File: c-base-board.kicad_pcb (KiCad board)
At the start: 2 copper layers, 49.1 x 49.1 mm, 172 parts

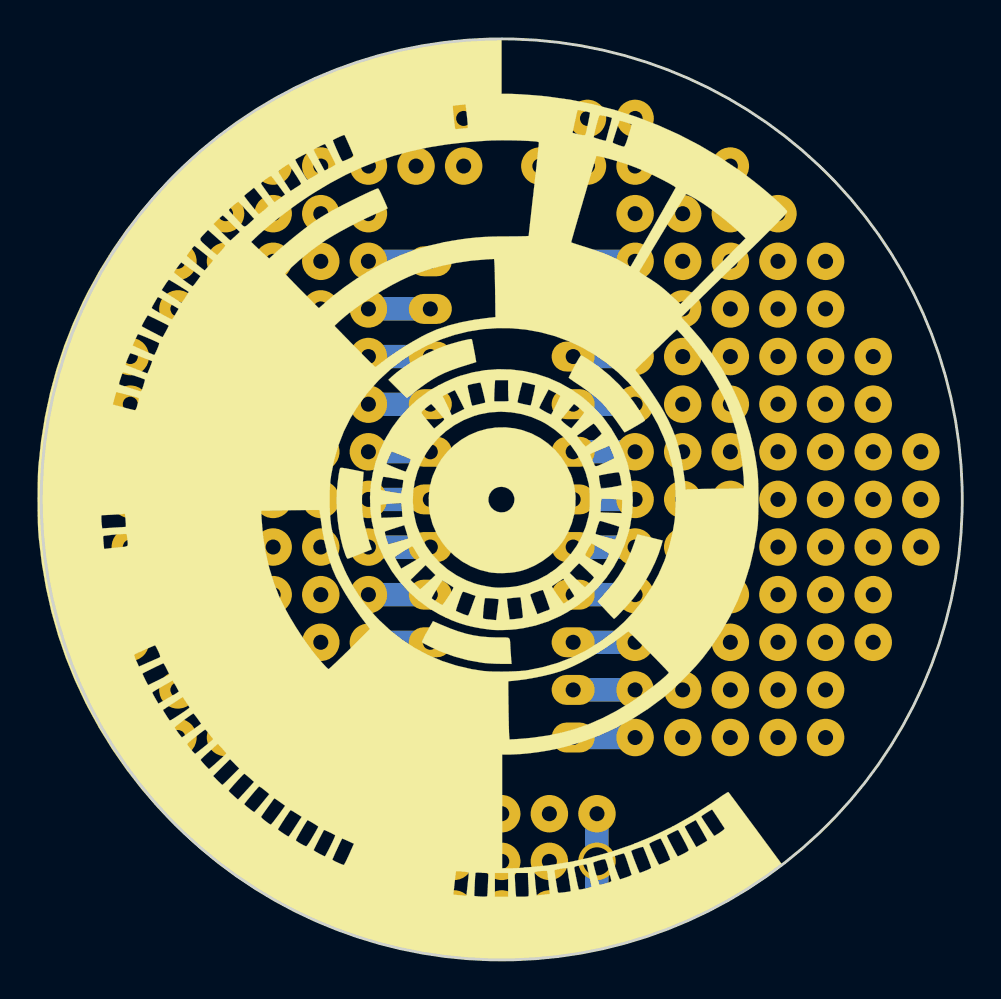
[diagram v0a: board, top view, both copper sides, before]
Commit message: improved revision
* 7805 support on bottom part
* ground and regulated volate bar at the sides
* no support for DIP28 packages
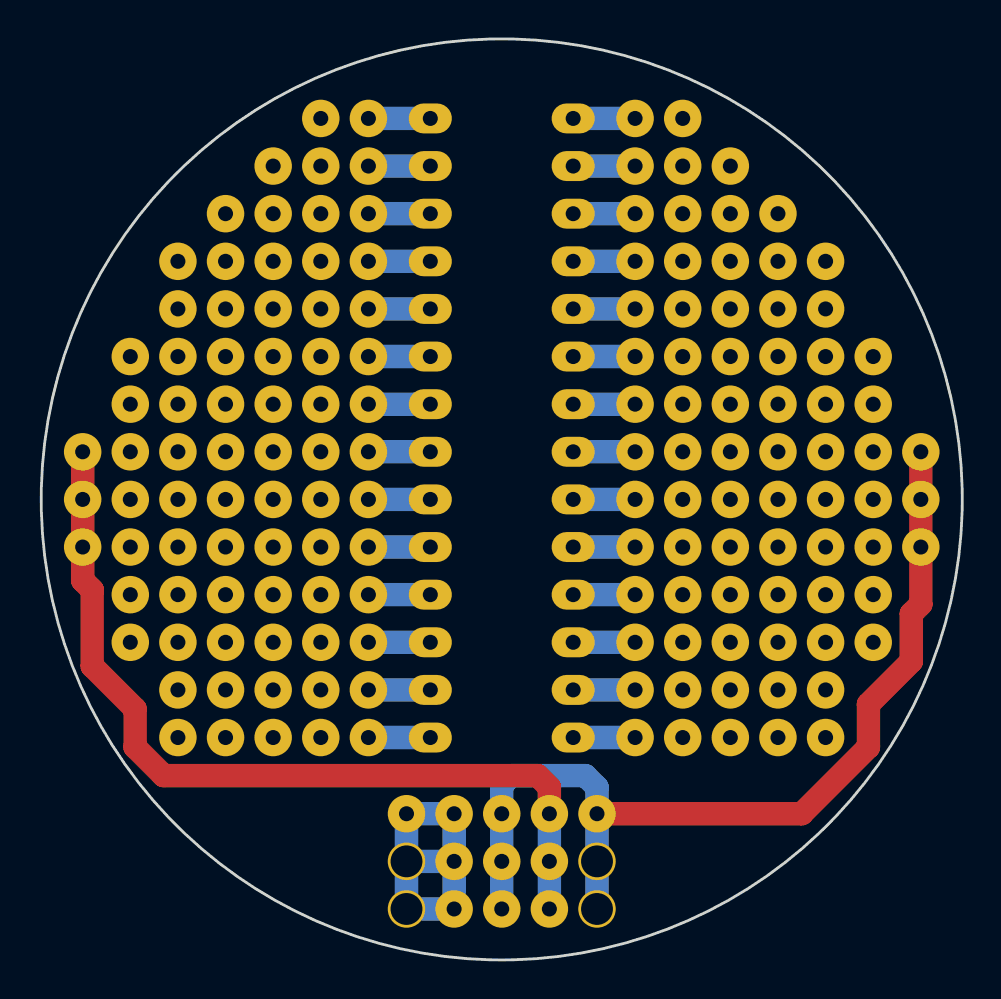
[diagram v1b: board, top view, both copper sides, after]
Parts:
- removed the G*** at (149.1, 123.4)
- removed the REF** at (145.3, 136.1)
- removed the REF**11 at (151.1, 103.1)
- removed the REF**11 at (153.7, 103.1)
- removed the REF**11 at (147.1, 103.1)
- removed the REF**11 at (147.1, 105.7)
- removed the REF**11 at (151.1, 105.7)
- removed the REF**11 at (153.7, 105.7)
- removed the REF**41 at (144.5, 103.1)
- removed the REF**41 at (144.5, 105.7)
- added REF**: DIP-28_W7.62mm_LongPads, Housings_DIP:DIP-28_W7.62mm_LongPads, B.Cu at (145.3, 136.1)
- added REF**21: SolderWirePad_single_0-8mmDrill, Wire_Pads:SolderWirePad_single_0-8mmDrill, F.Cu at (158.8, 103.1)
- added REF**31: SolderWirePad_single_0-8mmDrill, Wire_Pads:SolderWirePad_single_0-8mmDrill, F.Cu at (139.4, 103.1)
- moved G*** 3.05 mm to (149.1, 120.4)
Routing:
- net (no net): track 82.8 -> 208.1 mm
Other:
- board text added: "+"
- board text added: "rev-C"
- board text added: "⏚"
- board text removed: "rev-c"

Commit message: added c-base silkscreen
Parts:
- added G***: c-base, c-base-board:board-outline, F.Cu at (149.4, 123.4)

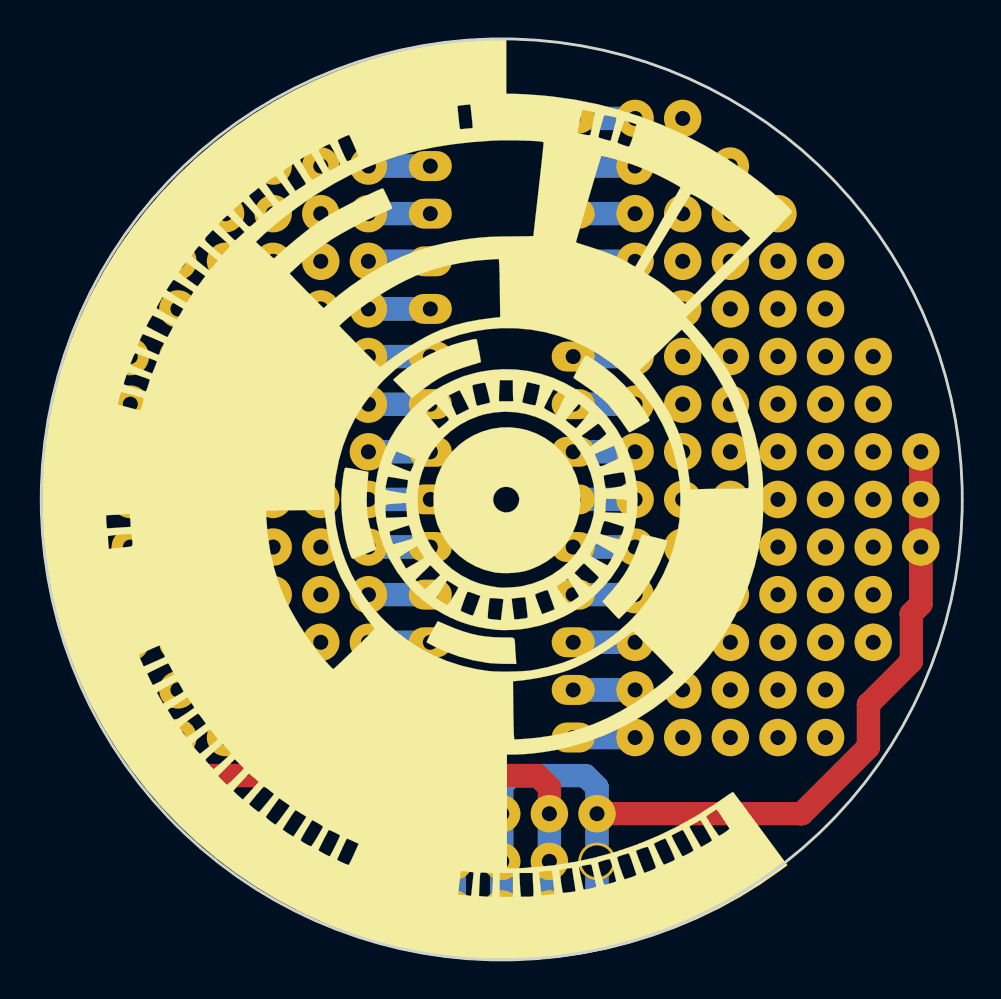
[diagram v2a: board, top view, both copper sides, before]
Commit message: added jumper spots for GND in voltage regulator area
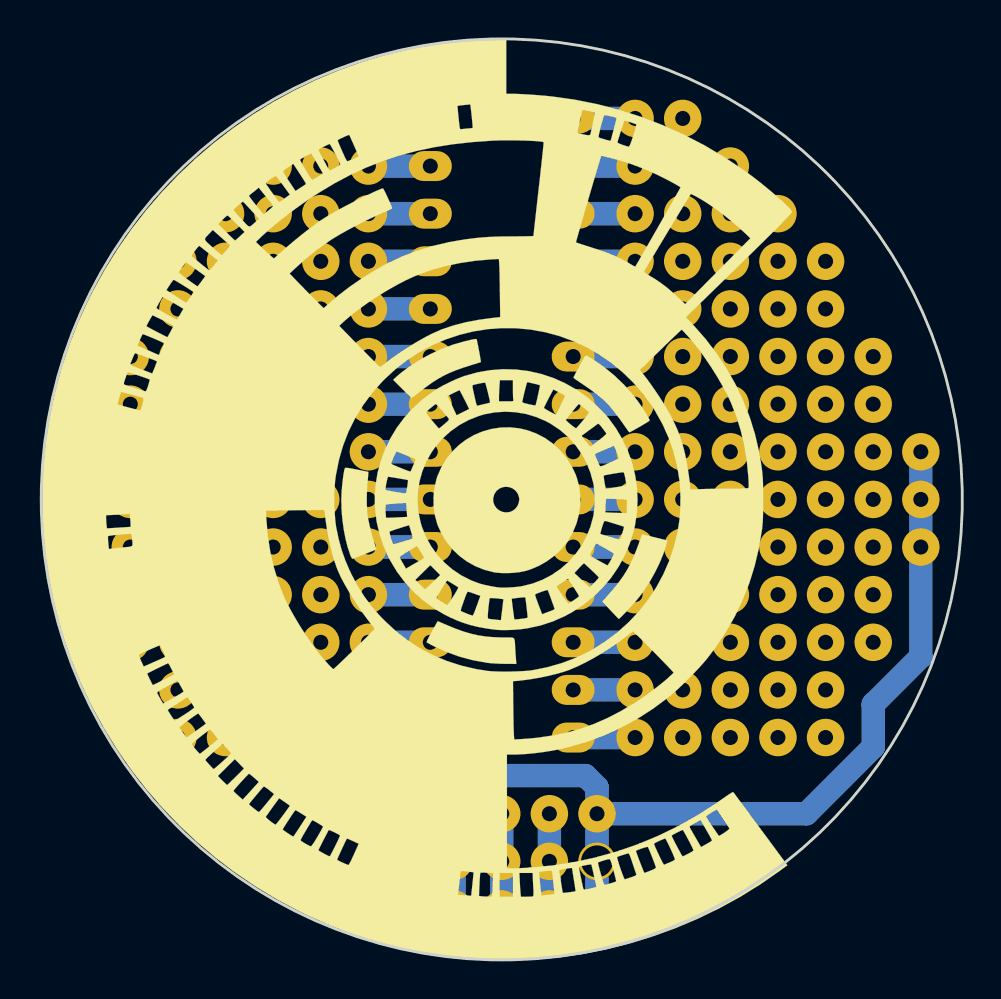
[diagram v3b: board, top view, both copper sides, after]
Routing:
- net (no net): track 208.1 -> 165.2 mm
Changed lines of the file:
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@@
     (area 124.461199 98.807199 173.734801 148.080801)
     (thickness 1.6)
-    (drawings 32)
-    (tracks 66)
+    (drawings 22)
+    (tracks 50)
     (zones 0)
     (modules 166)
@@
     (35 F.Paste user hide)
     (36 B.SilkS user)
-    (37 F.SilkS user)
-    (38 B.Mask user hide)
-    (39 F.Mask user hide)
+    (37 F.SilkS user hide)
+    (38 B.Mask user)
+    (39 F.Mask user)
     (40 Dwgs.User user hide)
     (41 Cmts.User user hide)
@@
       (xy -0.319227 -3.833328) (xy 0.178311 -3.845117) (xy 0.680572 -3.791698)) (layer F.SilkS) (width 0.01))
   )
+  (gr_text ⏚ (at 171.45 127.762) (layer B.SilkS)
+    (effects (font (size 1 1) (thickness 0.2)) (justify mirror))
+  )
+  (gr_line (start 151.638 138.938) (end 151.638 137.922) (layer B.Mask) (width 1))
+  (gr_line (start 149.098 138.938) (end 149.098 137.922) (layer B.Mask) (width 1))
+  (gr_line (start 146.558 138.938) (end 146.558 137.922) (layer B.Mask) (width 1))
   (dimension 49.276 (width 0.3) (layer Eco1.User)
     (gr_text "49,276 mm" (at 183.722 123.444 270) (layer Eco1.User)
@@
     (arrow2b (pts (xy 173.736 94.742) (xy 172.609496 95.328421)))
   )
-  (gr_line (start 126.746 129.794) (end 126.746 127.254) (layer B.SilkS) (width 0.2))
-  (gr_line (start 129.54 136.398) (end 126.746 129.794) (layer B.SilkS) (width 0.2))
-  (gr_line (start 131.064 137.922) (end 129.54 136.398) (layer B.SilkS) (width 0.2))
-  (gr_line (start 142.748 137.922) (end 131.064 137.922) (layer B.SilkS) (width 0.2))
-  (gr_line (start 142.748 138.938) (end 142.748 137.922) (layer B.SilkS) (width 0.2))
-  (gr_line (start 151.638 138.938) (end 142.748 138.938) (layer B.SilkS) (width 0.2))
-  (gr_line (start 151.638 139.192) (end 151.638 138.938) (layer B.SilkS) (width 0.2))
-  (gr_line (start 154.178 137.668) (end 154.178 138.938) (layer B.SilkS) (width 0.2))
-  (gr_line (start 155.448 137.668) (end 154.178 137.668) (layer B.SilkS) (width 0.2))
-  (gr_line (start 167.386 137.668) (end 155.448 137.668) (layer B.SilkS) (width 0.2))
-  (gr_line (start 170.688 132.334) (end 167.386 137.668) (layer B.SilkS) (width 0.2))
-  (gr_line (start 171.45 127.254) (end 170.688 132.334) (layer B.SilkS) (width 0.2))
-  (gr_text ⏚ (at 149.098 147.066) (layer B.SilkS)
+  (gr_text ⏚ (at 154.178 146.812) (layer B.SilkS)
     (effects (font (size 1 1) (thickness 0.2)) (justify mirror))
   )
-  (gr_text ⏚ (at 155.7274 138.2522) (layer B.SilkS)
-    (effects (font (size 1 1) (thickness 0.2)) (justify mirror))
-  )
-  (gr_text + (at 145.288 141.478) (layer B.SilkS)
+  (gr_text + (at 144.018 146.558) (layer B.SilkS)
     (effects (font (size 1 1) (thickness 0.2)) (justify mirror))
   )
@@
   (gr_line (start 125.476 119.634) (end 125.476 127.254) (layer B.SilkS) (width 0.2))
   (gr_line (start 170.18 127.254) (end 172.72 127.254) (layer B.SilkS) (width 0.2))
-  (gr_text + (at 145.288 144.018) (layer B.SilkS)
-    (effects (font (size 1 1) (thickness 0.2)) (justify mirror))
-  )
   (gr_text rev-C (at 138.684 141.478) (layer B.SilkS)
     (effects (font (size 1.5 1.5) (thickness 0.3)) (justify mirror))
@@
   )
   (gr_circle (center 149.098 123.444) (end 149.098 98.8822) (layer Edge.Cuts) (width 0.15))
-  (segment (start 144.018 142.748) (end 146.558 142.748) (width 1.25) (layer B.Cu) (net 0))
-  (segment (start 154.178 140.208) (end 165.1 140.208) (width 1.25) (layer F.Cu) (net 0))
-  (segment (start 165.1 140.208) (end 168.656 136.652) (width 1.25) (layer F.Cu) (net 0))
-  (segment (start 168.656 136.652) (end 168.656 134.366) (width 1.25) (layer F.Cu) (net 0))
-  (segment (start 168.656 134.366) (end 170.942 132.08) (width 1.25) (layer F.Cu) (net 0))
-  (segment (start 171.45 129.032) (end 171.45 125.984) (width 1.25) (layer F.Cu) (net 0))
-  (segment (start 170.942 132.08) (end 170.942 129.54) (width 1.25) (layer F.Cu) (net 0))
-  (segment (start 170.942 129.54) (end 171.45 129.032) (width 1.25) (layer F.Cu) (net 0))
-  (segment (start 126.746 125.984) (end 126.746 127.762) (width 1.25) (layer F.Cu) (net 0))
-  (segment (start 126.746 127.762) (end 127.254 128.27) (width 1.25) (layer F.Cu) (net 0))
-  (segment (start 151.019492 138.176) (end 151.638 138.794508) (width 1.25) (layer F.Cu) (net 0))
-  (segment (start 127.254 128.27) (end 127.254 132.334) (width 1.25) (layer F.Cu) (net 0))
-  (segment (start 127.254 132.334) (end 129.54 134.62) (width 1.25) (layer F.Cu) (net 0))
-  (segment (start 129.54 134.62) (end 129.54 136.652) (width 1.25) (layer F.Cu) (net 0))
-  (segment (start 151.638 138.794508) (end 151.638 140.208) (width 1.25) (layer F.Cu) (net 0))
-  (segment (start 129.54 136.652) (end 131.064 138.176) (width 1.25) (layer F.Cu) (net 0))
-  (segment (start 131.064 138.176) (end 151.019492 138.176) (width 1.25) (layer F.Cu) (net 0))
-  (segment (start 149.606 138.176) (end 149.098 138.684) (width 1.25) (layer B.Cu) (net 0))
-  (segment (start 149.098 138.684) (end 149.098 140.208) (width 1.25) (layer B.Cu) (net 0))
-  (segment (start 153.559492 138.176) (end 149.606 138.176) (width 1.25) (layer B.Cu) (net 0))
+  (segment (start 153.559492 138.176) (end 146.558 138.176) (width 1.25) (layer B.Cu) (net 0))
   (segment (start 154.178 140.208) (end 154.178 138.794508) (width 1.25) (layer B.Cu) (net 0))
   (segment (start 154.178 138.794508) (end 153.559492 138.176) (width 1.25) (layer B.Cu) (net 0))
-  (segment (start 126.746 123.444) (end 126.746 120.904) (width 1.25) (layer F.Cu) (net 0))
-  (segment (start 126.746 125.984) (end 126.746 123.444) (width 1.25) (layer F.Cu) (net 0))
-  (segment (start 171.45 123.444) (end 171.45 120.904) (width 1.25) (layer F.Cu) (net 0))
-  (segment (start 171.45 125.984) (end 171.45 123.444) (width 1.25) (layer F.Cu) (net 0))
+  (segment (start 154.178 140.208) (end 165.354 140.208) (width 1.25) (layer B.Cu) (net 0))
+  (segment (start 168.91 136.652) (end 168.91 134.366) (width 1.25) (layer B.Cu) (net 0))
+  (segment (start 168.91 134.366) (end 171.45 131.826) (width 1.25) (layer B.Cu) (net 0))
+  (segment (start 165.354 140.208) (end 168.91 136.652) (width 1.25) (layer B.Cu) (net 0))
+  (segment (start 171.45 131.826) (end 171.45 125.984) (width 1.25) (layer B.Cu) (net 0))
+  (segment (start 126.746 123.444) (end 126.746 125.984) (width 1.25) (layer B.Cu) (net 0))
+  (segment (start 126.746 120.904) (end 126.746 123.444) (width 1.25) (layer B.Cu) (net 0))
+  (segment (start 171.45 125.984) (end 171.45 123.444) (width 1.25) (layer B.Cu) (net 0))
+  (segment (start 171.45 120.904) (end 171.45 123.444) (width 1.25) (layer B.Cu) (net 0))
   (segment (start 145.288 136.144) (end 141.986 136.144) (width 1.25) (layer B.Cu) (net 0))
   (segment (start 141.986 133.604) (end 145.288 133.604) (width 1.25) (layer B.Cu) (net 0))
@@
   (segment (start 152.908 133.604) (end 156.21 133.604) (width 1.25) (layer B.Cu) (net 0))
   (segment (start 152.908 136.144) (end 156.21 136.144) (width 1.25) (layer B.Cu) (net 0))
-  (segment (start 144.018 145.288) (end 146.558 145.288) (width 1.25) (layer B.Cu) (net 0))
-  (segment (start 144.018 140.208) (end 146.558 140.208) (width 1.25) (layer B.Cu) (net 0))
   (segment (start 144.018 142.748) (end 144.018 140.208) (width 1.25) (layer B.Cu) (net 0))
   (segment (start 151.638 142.748) (end 151.638 140.208) (width 1.25) (layer B.Cu) (net 0))

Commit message: new revision - orderd from dirtypcb
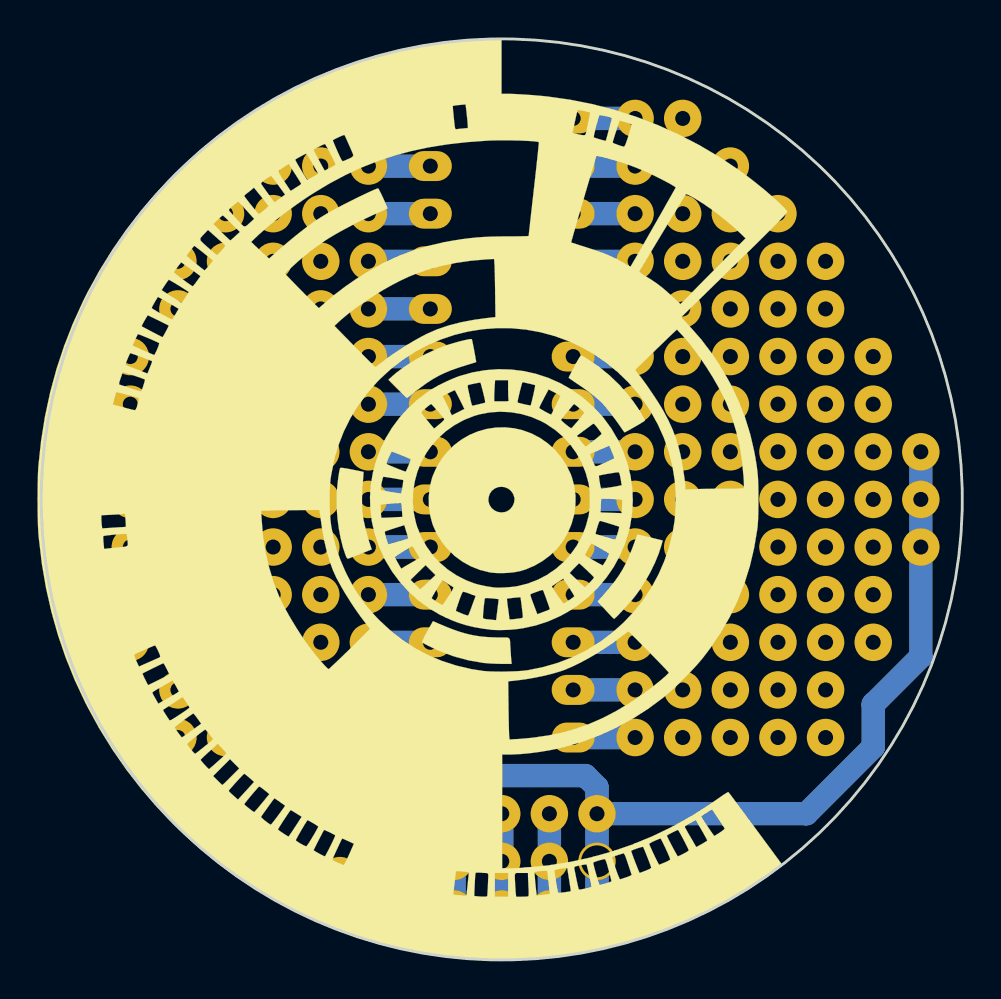
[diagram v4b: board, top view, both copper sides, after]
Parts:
- added REF**1111: SolderWirePad_single_0-8mmDrill, Wire_Pads:SolderWirePad_single_0-8mmDrill, F.Cu at (140.5, 143.5)
- moved G*** 0.25 mm to (149.1, 123.4)
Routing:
- net (no net): track 165.2 -> 190.8 mm
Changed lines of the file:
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@@
-(kicad_pcb (version 4) (host pcbnew 4.0.1-3.201512221401+6198~38~ubuntu15.10.1-stable)
+(kicad_pcb (version 4) (host pcbnew 4.0.2-4+6225~38~ubuntu15.10.1-stable)
   (general
     (links 0)
     (no_connects 0)
-    (area 124.461199 98.807199 173.734801 148.080801)
+    (area 113.661475 91.892 190.372 148.803)
     (thickness 1.6)
     (drawings 22)
-    (tracks 50)
+    (tracks 55)
     (zones 0)
-    (modules 166)
+    (modules 167)
     (nets 1)
   )
@@
     (35 F.Paste user hide)
     (36 B.SilkS user)
-    (37 F.SilkS user hide)
+    (37 F.SilkS user)
     (38 B.Mask user)
     (39 F.Mask user)
@@
       (layerselection 0x010f0_80000001)
       (usegerberextensions true)
-      (excludeedgelayer true)
+      (excludeedgelayer false)
       (linewidth 0.100000)
       (plotframeref false)
@@
     (uvia_dia 0.3)
     (uvia_drill 0.1)
+  )
+  (module Wire_Pads:SolderWirePad_single_0-8mmDrill (layer F.Cu)
+    (at 140.462 143.51)
+    (fp_text reference REF**1111 (at 0 -2.54) (layer F.SilkS) hide
+      (effects (font (size 1 1) (thickness 0.15)))
+    )
+    (fp_text value SolderWirePad_single_0-8mmDrill (at 0 2.54) (layer F.Fab) hide
+      (effects (font (size 1 1) (thickness 0.15)))
+    )
+    (pad 1 thru_hole circle (at 0 0) (size 1.99898 1.99898) (drill 0.8001) (layers *.Cu *.Mask F.SilkS))
   )
   (module Wire_Pads:SolderWirePad_single_0-8mmDrill (layer F.Cu)
@@
   )
   (module c-base-board:board-outline (layer F.Cu)
-    (at 149.352 123.444)
+    (at 149.098 123.444)
     (fp_text reference G*** (at 0.3048 -2.5146) (layer F.SilkS) hide
       (effects (font (thickness 0.3)))
@@
   (gr_line (start 125.476 119.634) (end 125.476 127.254) (layer B.SilkS) (width 0.2))
   (gr_line (start 170.18 127.254) (end 172.72 127.254) (layer B.SilkS) (width 0.2))
-  (gr_text rev-C (at 138.684 141.478) (layer B.SilkS)
+  (gr_text rev-C (at 138.684 140.97) (layer B.SilkS)
     (effects (font (size 1.5 1.5) (thickness 0.3)) (justify mirror))
   )
-  (gr_text c-lab (at 138.684 139.7) (layer B.SilkS)
+  (gr_text c-lab (at 138.684 138.938) (layer B.SilkS)
     (effects (font (size 1.5 1.5) (thickness 0.3)) (justify mirror))
   )
@@
   )
   (gr_circle (center 149.098 123.444) (end 149.098 98.8822) (layer Edge.Cuts) (width 0.15))
+  (segment (start 126.746 125.984) (end 126.746 131.826) (width 1.25) (layer B.Cu) (net 0))
+  (segment (start 126.746 131.826) (end 129.286 134.366) (width 1.25) (layer B.Cu) (net 0))
+  (segment (start 129.286 134.366) (end 129.286 136.398) (width 1.25) (layer B.Cu) (net 0))
+  (segment (start 129.286 136.398) (end 136.398 143.51) (width 1.25) (layer B.Cu) (net 0))
+  (segment (start 136.398 143.51) (end 140.462 143.51) (width 1.25) (layer B.Cu) (net 0))
   (segment (start 153.559492 138.176) (end 146.558 138.176) (width 1.25) (layer B.Cu) (net 0))
   (segment (start 154.178 140.208) (end 154.178 138.794508) (width 1.25) (layer B.Cu) (net 0))
